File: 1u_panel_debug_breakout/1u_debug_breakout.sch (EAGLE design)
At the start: 7 parts, among them J1 1.27MM-SWD-CONNECTOR

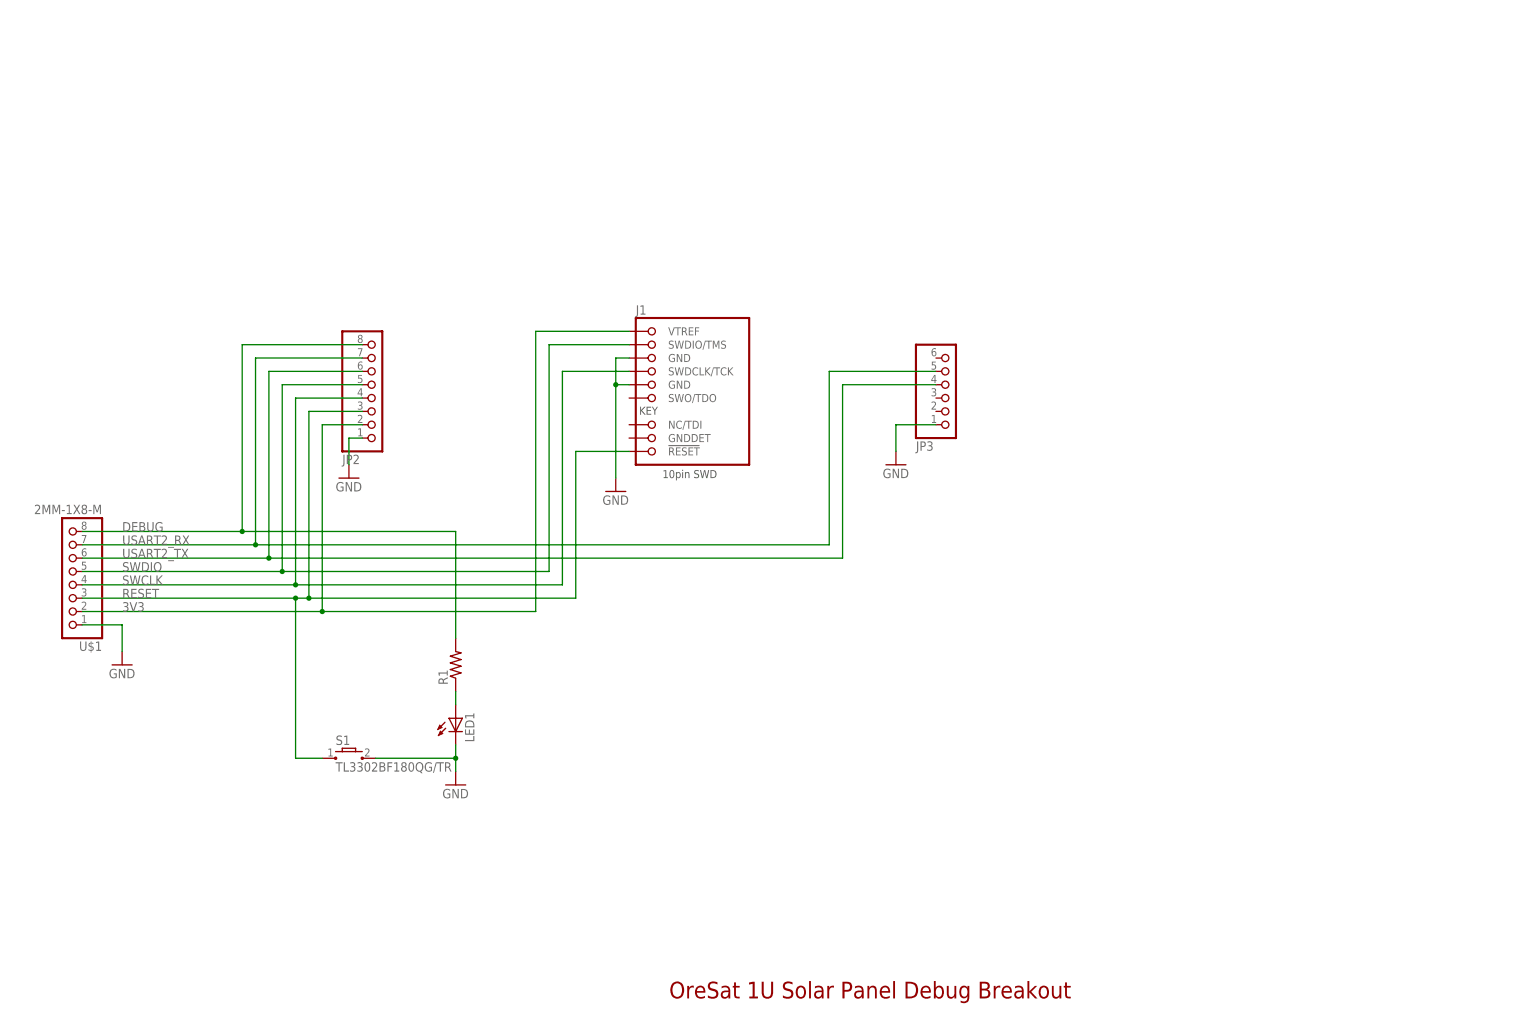
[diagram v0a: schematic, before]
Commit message: Update solar panel debugging board for v2.
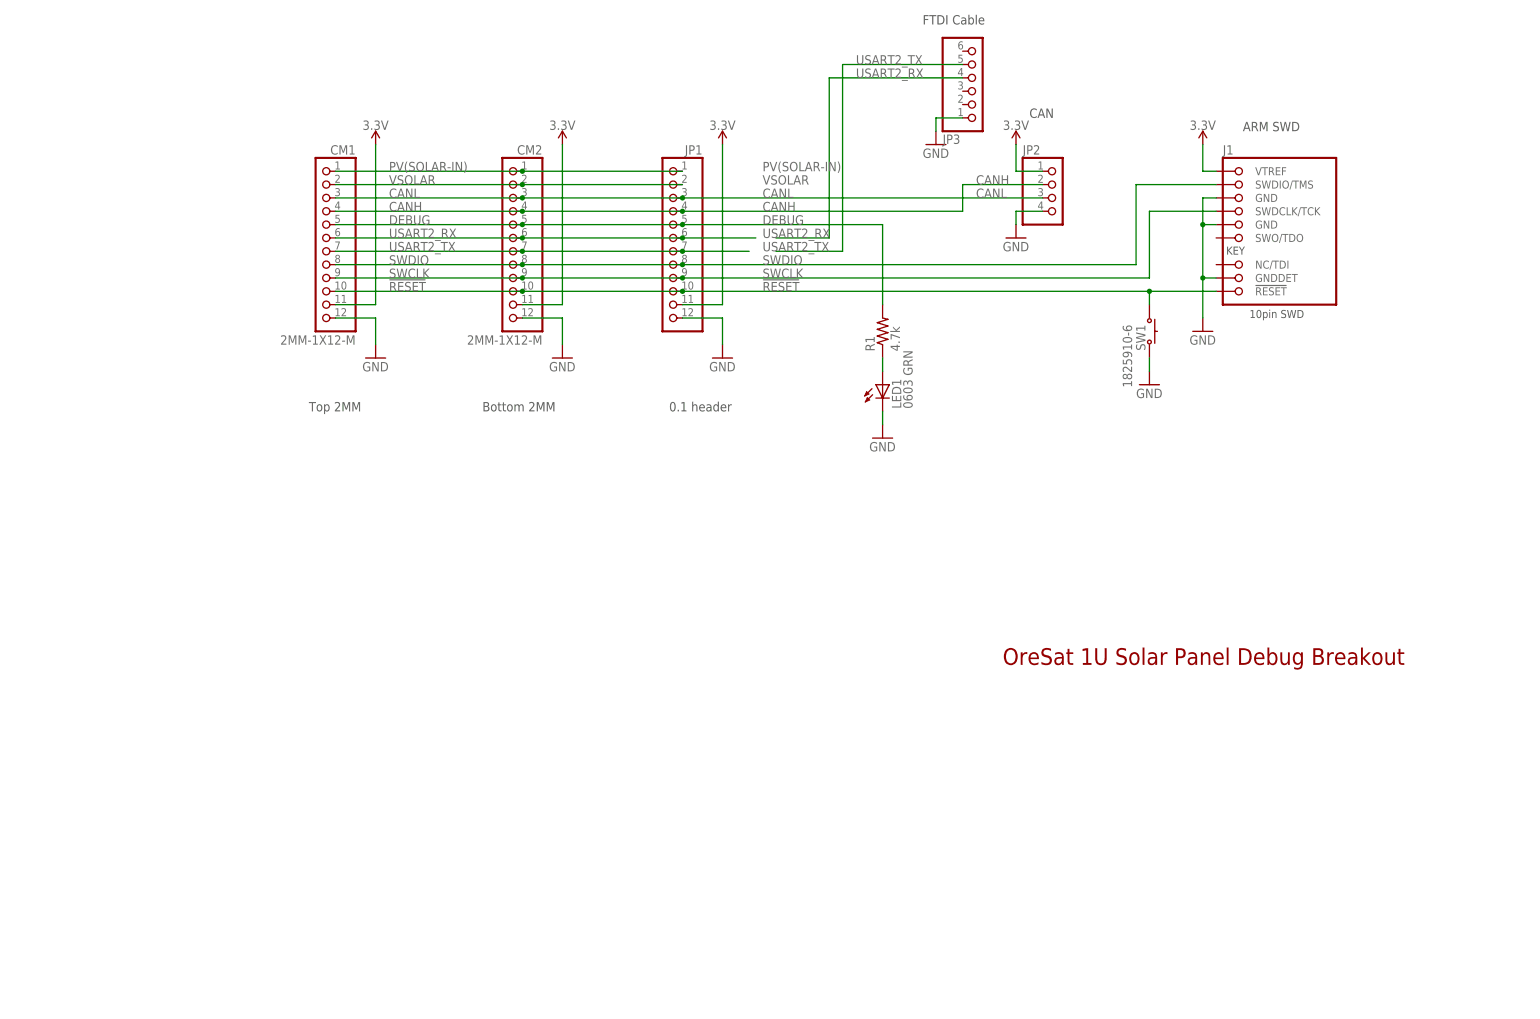
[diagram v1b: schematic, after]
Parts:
- removed S1: TL3302BF180QG/TR, eswitch-tact:TL3302-G
- removed U$1: 2MM-1X8-M, 2mm-RA-solar-module-debugging:2MM-1X8-M
- added CM1, CM2: 2MM-1X12-M, J-precidip-880-2mm:2MM-1X12-M
- added JP1: (no value), pinhead:PINHD-1X12
- added SW1: 1825910-6, SW-TE-1825910-6mm-switch:1825910-6
- JP2: device pinhead:PINHD-1X8 -> pinhead:PINHD-1X4
- LED1: value (none) -> 0603 GRN
- R1: value (none) -> 4.7k
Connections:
- removed net 3V3: J1.VTREF, JP2.2, U$1.2
- removed net RESET: J1.!RESET, JP2.3, S1.1, U$1.3
- new net !RESET: CM1.10, CM2.10, J1.!RESET, JP1.10, SW1.1
- new net 3.3V: CM1.11, CM2.11, J1.VTREF, JP1.11, JP2.1
- new net CANH: CM1.4, CM2.4, JP1.4, JP2.2
- new net CANL: CM1.3, CM2.3, JP1.3, JP2.3
- new net PV(SOLAR-IN): CM1.1, CM2.1, JP1.1
- new net VSOLAR: CM1.2, CM2.2, JP1.2
- net DEBUG: now also CM1.5, CM2.5, JP1.5; no longer JP2.8, U$1.8
- net GND: now also CM1.12, CM2.12, J1.GNDDET, JP1.12, JP2.4, SW1.2; no longer JP2.1, S1.2, U$1.1
- net SWCLK: now also CM1.9, CM2.9, JP1.9; no longer JP2.4, U$1.4
- net SWDIO: now also CM1.8, CM2.8, JP1.8; no longer JP2.5, U$1.5
- net USART2_RX: now also CM1.6, CM2.6, JP1.6, JP3.4; no longer JP2.7, JP3.5, U$1.7
- net USART2_TX: now also CM1.7, CM2.7, JP1.7, JP3.5; no longer JP2.6, JP3.4, U$1.6
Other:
- note added: "0.1 header"
- note added: "ARM SWD"
- note added: "Bottom 2MM"
- note added: "CAN"
- note added: "FTDI Cable"
- note added: "Top 2MM"
- moved on the sheet: J1, JP3, LED1, R1

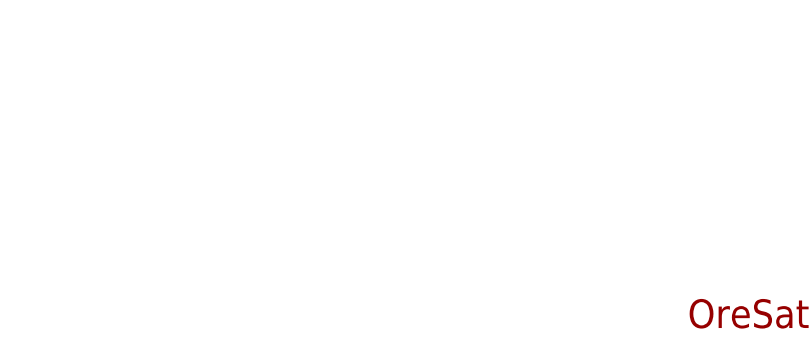
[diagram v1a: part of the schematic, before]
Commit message: Fixed breakout connector to solar panel, added scope clips.
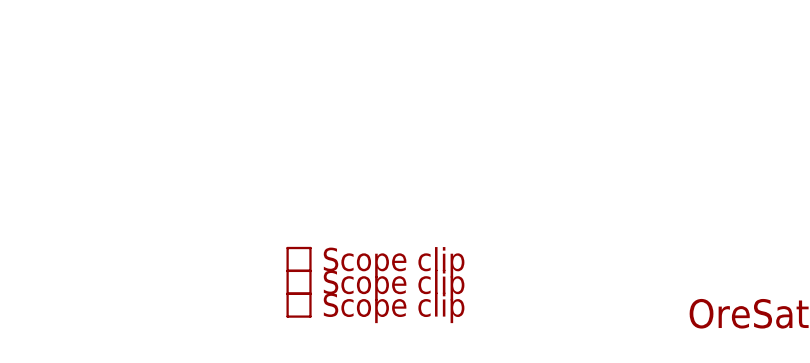
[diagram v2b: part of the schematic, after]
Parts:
- added U$1, U$2, U$3: SCOPE_CLIP, oresat-misc:SCOPE_CLIP
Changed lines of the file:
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@@
 <part name="SUPPLY5" library="SparkFun-PowerSymbols" library_urn="urn:adsk.eagle:library:530" deviceset="3.3V" device=""/>
 <part name="SW1" library="SW-TE-1825910-6mm-switch" deviceset="1825910-6" device=""/>
+<part name="U$1" library="oresat-misc" deviceset="SCOPE_CLIP" device=""/>
+<part name="U$2" library="oresat-misc" deviceset="SCOPE_CLIP" device=""/>
+<part name="U$3" library="oresat-misc" deviceset="SCOPE_CLIP" device=""/>
 </parts>
 <sheets>
@@
 <instance part="SUPPLY5" gate="G$1" x="177.8" y="127"/>
 <instance part="SW1" gate="A" x="203.2" y="91.44" rot="R270"/>
+<instance part="U$1" gate="G$1" x="132.08" y="35.56"/>
+<instance part="U$2" gate="G$1" x="132.08" y="33.02"/>
+<instance part="U$3" gate="G$1" x="132.08" y="30.48"/>
 </instances>
 <busses>

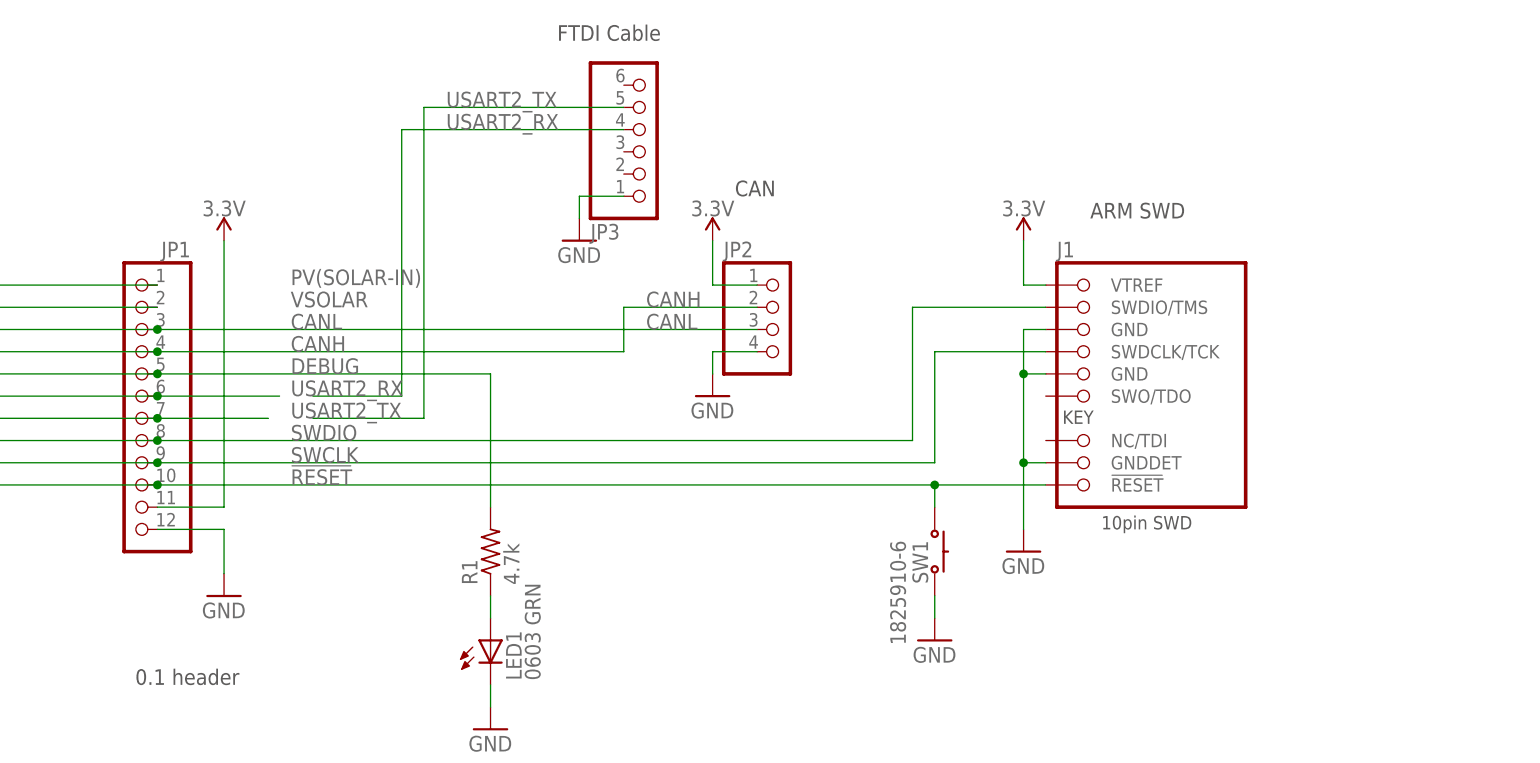
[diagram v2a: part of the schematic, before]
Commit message: Added part numbers to odd connectors.
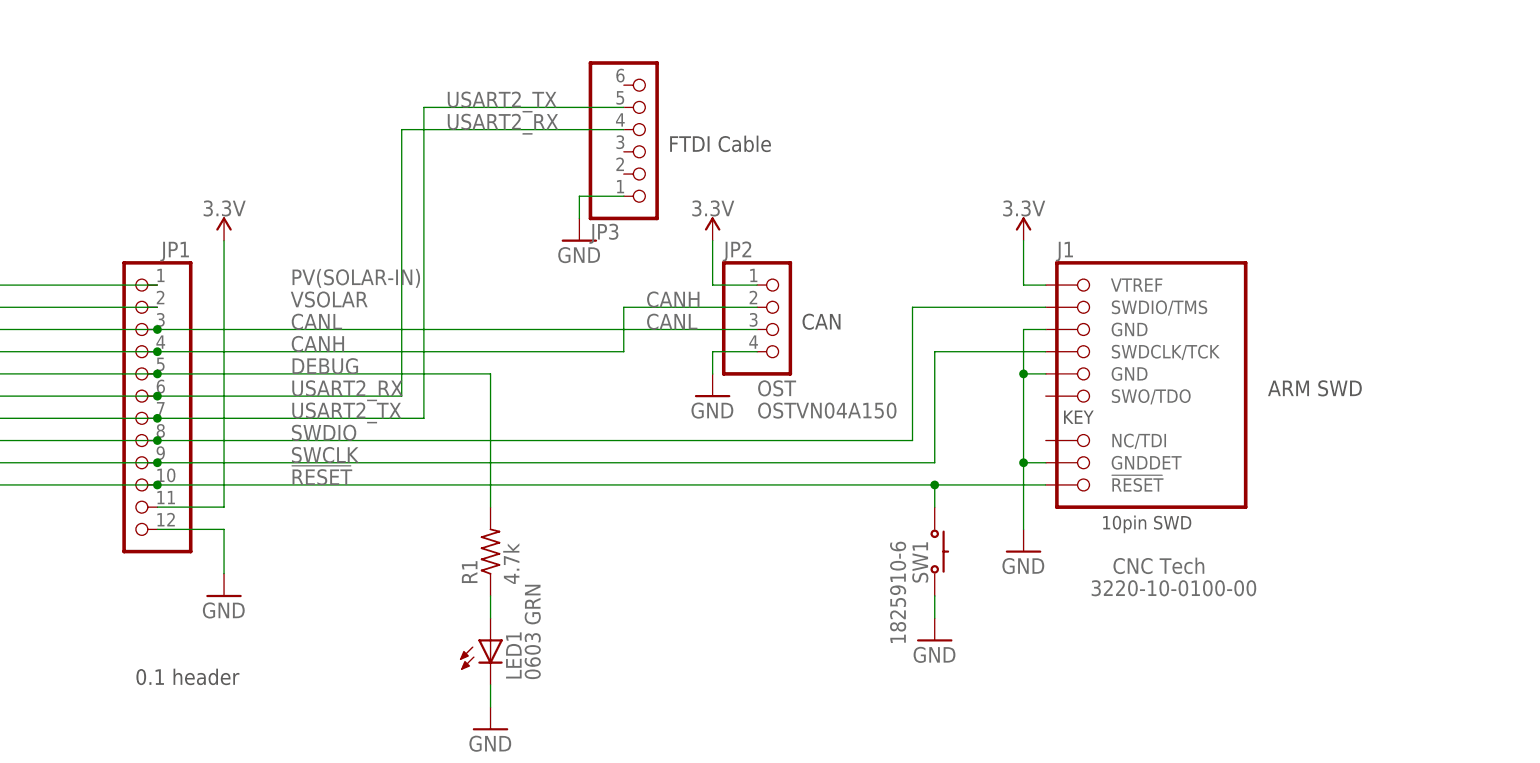
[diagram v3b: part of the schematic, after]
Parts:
- J1: device con-swd:1.27MM-SWD-CONNECTOR -> J-CNC-3220-10-0100-00-ARM-SWD-port:1.27MM-SWD-CONNECTOR; DIS (none) -> Digi-Key; DPN (none) -> 1175-1627-ND; MFR (none) -> CNC Tech; MPN (none) -> 3220-10-0100-00
- JP2: DIS (none) -> Digi-Key; DPN (none) -> ED10563-ND; MFR (none) -> OST; MPN (none) -> OSTVN04A150
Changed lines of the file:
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@@
 <setting verticaltext="up"/>
 </settings>
-<grid distance="0.1" unitdist="inch" unit="inch" style="lines" multiple="1" display="no" altdistance="0.01" altunitdist="inch" altunit="inch"/>
+<grid distance="0.05" unitdist="inch" unit="inch" style="lines" multiple="2" display="no" altdistance="0.01" altunitdist="inch" altunit="inch"/>
 <layers>
 <layer number="1" name="Top" color="4" fill="1" visible="no" active="no"/>
@@
 <part name="FRAME1" library="frames" deviceset="FRAME_A_L" device=""/>
 <part name="GND1" library="supply1" deviceset="GND" device=""/>
-<part name="J1" library="con-swd" deviceset="1.27MM-SWD-CONNECTOR" device=""/>
+<part name="J1" library="J-CNC-3220-10-0100-00-ARM-SWD-port" deviceset="1.27MM-SWD-CONNECTOR" device="">
+<attribute name="DIS" value="Digi-Key"/>
+<attribute name="DPN" value="1175-1627-ND"/>
+<attribute name="MFR" value="CNC Tech"/>
+<attribute name="MPN" value="3220-10-0100-00"/>
+</part>
 <part name="R1" library="resistor" deviceset="R-US_" device="R0603" value="4.7k"/>
 <part name="GND3" library="supply1" deviceset="GND" device=""/>
@@
 <part name="GND2" library="supply1" deviceset="GND" device=""/>
 <part name="SUPPLY4" library="SparkFun-PowerSymbols" library_urn="urn:adsk.eagle:library:530" deviceset="3.3V" device=""/>
-<part name="JP2" library="pinhead" library_urn="urn:adsk.eagle:library:325" deviceset="PINHD-1X4" device="" package3d_urn="urn:adsk.eagle:package:22407/2"/>
+<part name="JP2" library="pinhead" library_urn="urn:adsk.eagle:library:325" deviceset="PINHD-1X4" device="" package3d_urn="urn:adsk.eagle:package:22407/2">
+<attribute name="DIS" value="Digi-Key"/>
+<attribute name="DPN" value="ED10563-ND"/>
+<attribute name="MFR" value="OST"/>
+<attribute name="MPN" value="OSTVN04A150"/>
+</part>
 <part name="GND8" library="supply1" deviceset="GND" device=""/>
 <part name="SUPPLY5" library="SparkFun-PowerSymbols" library_urn="urn:adsk.eagle:library:530" deviceset="3.3V" device=""/>
@@
 <text x="76.2" y="76.2" size="1.778" layer="97">Bottom 2MM</text>
 <text x="111.76" y="76.2" size="1.778" layer="97">0.1 header</text>
-<text x="160.02" y="149.86" size="1.778" layer="97">FTDI Cable</text>
-<text x="220.98" y="129.54" size="1.778" layer="97">ARM SWD</text>
-<text x="180.34" y="132.08" size="1.778" layer="97">CAN</text>
+<text x="172.72" y="137.16" size="1.778" layer="97">FTDI Cable</text>
+<text x="187.96" y="116.84" size="1.778" layer="97">CAN</text>
+<text x="241.3" y="109.22" size="1.778" layer="97">ARM SWD</text>
 </plain>
 <instances>
@@
 <instance part="FRAME1" gate="G$2" x="172.72" y="0"/>
 <instance part="GND1" gate="1" x="55.88" y="86.36"/>
-<instance part="J1" gate="J" x="226.06" y="111.76"/>
+<instance part="J1" gate="J" x="226.06" y="111.76">
+<attribute name="DIS" x="226.06" y="111.76" size="1.778" layer="96" display="off"/>
+<attribute name="DPN" x="226.06" y="111.76" size="1.778" layer="96" display="off"/>
+<attribute name="MFR" x="223.52" y="88.9" size="1.778" layer="96"/>
+<attribute name="MPN" x="220.98" y="86.36" size="1.778" layer="96"/>
+</instance>
 <instance part="R1" gate="G$1" x="152.4" y="91.44" rot="R90"/>
 <instance part="GND3" gate="1" x="152.4" y="71.12"/>
@@
 <instance part="GND2" gate="1" x="203.2" y="81.28"/>
 <instance part="SUPPLY4" gate="G$1" x="213.36" y="127"/>
-<instance part="JP2" gate="A" x="185.42" y="116.84"/>
+<instance part="JP2" gate="A" x="185.42" y="116.84">
+<attribute name="DIS" x="185.42" y="116.84" size="1.778" layer="96" display="off"/>
+<attribute name="DPN" x="185.42" y="116.84" size="1.778" layer="96" display="off"/>
+<attribute name="MFR" x="182.88" y="109.22" size="1.778" layer="96"/>
+<attribute name="MPN" x="182.88" y="106.68" size="1.778" layer="96"/>
+</instance>
 <instance part="GND8" gate="1" x="177.8" y="109.22"/>
 <instance part="SUPPLY5" gate="G$1" x="177.8" y="127"/>
@@
 <net name="USART2_RX" class="0">
 <segment>
-<wire x1="132.08" y1="109.22" x2="142.24" y2="109.22" width="0.1524" layer="91"/>
-<wire x1="142.24" y1="109.22" x2="142.24" y2="139.7" width="0.1524" layer="91"/>
-<label x="147.32" y="139.7" size="1.778" layer="95"/>
-<pinref part="JP3" gate="A" pin="4"/>
-<wire x1="142.24" y1="139.7" x2="167.64" y2="139.7" width="0.1524" layer="91"/>
-</segment>
-<segment>
-<wire x1="114.3" y1="109.22" x2="128.27" y2="109.22" width="0.1524" layer="91"/>
+<wire x1="114.3" y1="109.22" x2="142.24" y2="109.22" width="0.1524" layer="91"/>
 <label x="129.54" y="109.22" size="1.778" layer="95"/>
 <pinref part="JP1" gate="G$1" pin="6"/>
@@
 <wire x1="114.3" y1="109.22" x2="83.82" y2="109.22" width="0.1524" layer="91"/>
 <junction x="114.3" y="109.22"/>
+<wire x1="142.24" y1="109.22" x2="142.24" y2="139.7" width="0.1524" layer="91"/>
+<label x="147.32" y="139.7" size="1.778" layer="95"/>
+<pinref part="JP3" gate="A" pin="4"/>
+<wire x1="142.24" y1="139.7" x2="167.64" y2="139.7" width="0.1524" layer="91"/>
 </segment>
 </net>
 <net name="USART2_TX" class="0">
 <segment>
-<wire x1="132.08" y1="106.68" x2="144.78" y2="106.68" width="0.1524" layer="91"/>
 <wire x1="144.78" y1="106.68" x2="144.78" y2="142.24" width="0.1524" layer="91"/>
 <label x="147.32" y="142.24" size="1.778" layer="95"/>
 <pinref part="JP3" gate="A" pin="5"/>
 <wire x1="144.78" y1="142.24" x2="167.64" y2="142.24" width="0.1524" layer="91"/>
-</segment>
-<segment>
 <pinref part="CM1" gate="G$1" pin="7"/>
 <label x="58.42" y="106.68" size="1.778" layer="95"/>
@@
 <wire x1="48.26" y1="106.68" x2="83.82" y2="106.68" width="0.1524" layer="91"/>
 <junction x="83.82" y="106.68"/>
-<wire x1="114.3" y1="106.68" x2="127" y2="106.68" width="0.1524" layer="91"/>
+<wire x1="114.3" y1="106.68" x2="144.78" y2="106.68" width="0.1524" layer="91"/>
 <label x="129.54" y="106.68" size="1.778" layer="95"/>
 <pinref part="JP1" gate="G$1" pin="7"/>
